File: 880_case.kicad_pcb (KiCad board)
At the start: 2 copper layers, 316.8 x 38 mm, 178 parts, among them CON1 BARREL_JACK, J1 RUN/STOP, J10 RS IN, J11 CP IN, J12 MA IN, J13 CB IN, J14 CY IN, J15 OH IN, J16 CH IN, J17 IN 1, J18 IN 2, J19 IN 3, J2 SYNC24 CLK, J20 IN 4, J21 MULT IN, J22 SUM, J23 JACK_STEREO, J24 JACK_TRS_SWITCHED, J3 ASSIGN 1, J4 ASSIGN 2, J5 BD IN, J6 SD IN, J7 LT IN, J8 MT IN, J9 HT IN, P1 CONN_02X03, P2 CONN_01X02, P3 CONN_02X05, P4 CONN_01X03, P5 CONN_01X04, P6 CONN_01X04, P7 CONN_01X03, P8 CONN_01X03, P9 CONN_01X03, Q1 MMBT3904, Q10 MMBT3904, Q11 MMBT3904, Q12 MMBT3904, Q13 MMBT3904, Q14 C945, Q15 A733, Q2 MMBT3904, Q3 MMBT3904, Q4 MMBT3904, Q5 MMBT3904, Q6 MMBT3904, Q7 MMBT3904, Q8 MMBT3904, Q9 MMBT3904, U1 74HC165, U2 74HC165, U3 VX078-500, U4 VX078-500, U5 4558, U6 4558, X1 MIDI OUT, X2 SYNC24

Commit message: working on second revision, about to move headhpone amp circuit to align board-to-board connectors
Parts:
- P3: footprint w_conn_strip:vasch_strip_5x2 -> w_conn_strip:vasch_strip_8x2
- U5, U6: footprint Housings_SSOP:TSSOP-8_3x3mm_Pitch0.65mm -> Housings_SSOP:TSSOP-8_4.4x3mm_Pitch0.65mm
- moved P5 25.4 mm to (263.6, 88.5)
- moved R67 25.4 mm to (258.6, 85.0)
- moved C17 24.1 mm to (258.4, 117.5)
- moved D21 23.3 mm to (255.9, 110.5)
- moved Q14 23.3 mm to (254.7, 114.5)
- moved Q15 23.3 mm to (251.7, 110.5)
- moved R59 23.3 mm to (254.4, 110.7)
- moved R61 23.3 mm to (251.7, 115.5)
- moved R62 23.3 mm to (252.7, 107.5)
- moved C18 23.3 mm to (262.9, 111.5)
- moved D20 23.3 mm to (257.4, 110.5)
- moved R58 23.3 mm to (257.4, 114.2)
- moved R63 23.3 mm to (256.6, 107.5)
- moved R64 23.3 mm to (256.6, 105.5)
- moved U6 22.6 mm to (260.4, 112.0)
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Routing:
- net Net-(P7-Pad2): track 21.8 -> 2.27 mm, vias 1 -> 0
- net Net-(J21-Pad2): track 33.2 -> 16.3 mm
- net Net-(P7-Pad1): track 12.0 -> 6.47 mm
- net -V: track 313.8 -> 317.9 mm, vias 4 -> 3
- net GND: track 88.0 -> 84.0 mm, vias 19 -> 17
- net Net-(C5-Pad1): track 41.8 -> 45.3 mm
- net Net-(C6-Pad2): track 8.50 -> 11.8 mm
- net +V: track 272.0 -> 274.2 mm
- net Net-(C15-Pad2): track 12.6 -> 10.6 mm
- net Net-(R1-Pad1): track 50.5 -> 52.2 mm
- net (no net): track 0.00 -> 1.63 mm
- net Net-(D20-Pad1): track 36.6 -> 35.8 mm
- net Net-(C12-Pad1): track 13.5 -> 14.3 mm
- net Net-(C16-Pad1): track 68.6 -> 67.8 mm
- net Net-(C11-Pad1): track 8.79 -> 9.47 mm
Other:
- board text added: "880 case board r1.1 6/2019"
- board text removed: "880 case board r1.0 2/2019"

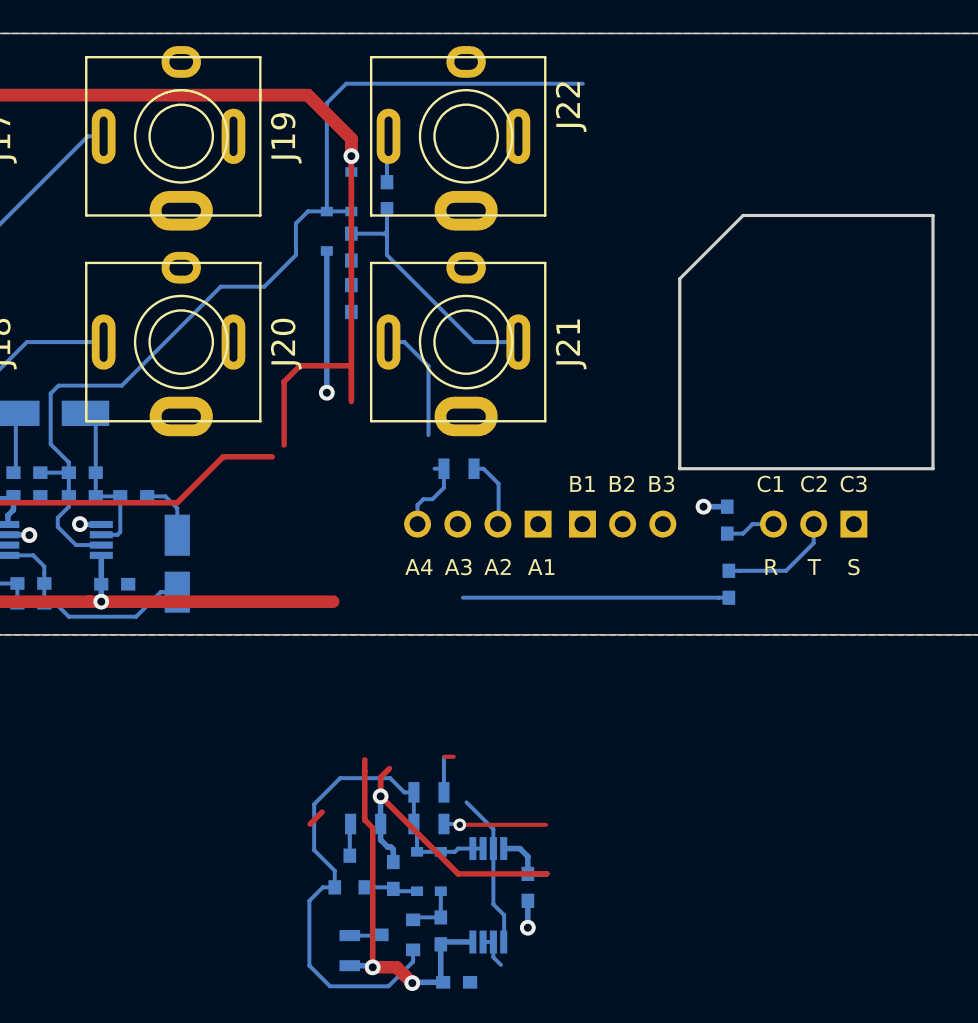
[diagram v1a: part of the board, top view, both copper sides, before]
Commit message: headphone amp components moved
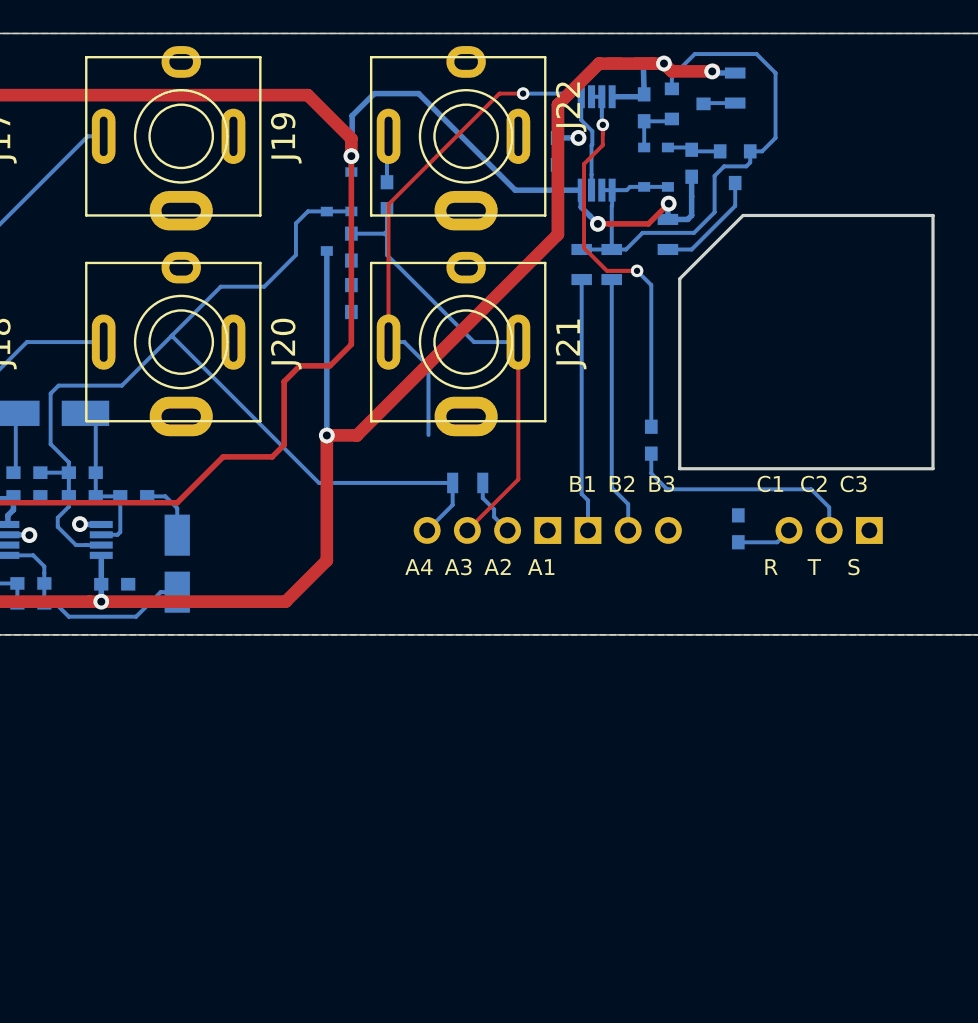
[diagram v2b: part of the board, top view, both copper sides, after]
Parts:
- moved R61 59.7 mm to (276.0, 61.0), turned to 270 degrees
- moved C17 59.0 mm to (269.2, 59.4), turned to 180 degrees
- moved Q14 55.6 mm to (273.0, 62.0), turned to 0 degrees
- moved R58 53.6 mm to (270.2, 62.2), turned to 270 degrees
- moved Q15 50.7 mm to (276.0, 66.0), turned to 270 degrees
- moved R59 48.8 mm to (273.2, 65.7), turned to 90 degrees
- moved U6 48.0 mm to (267.2, 64.5), turned to 90 degrees
- moved D21 47.2 mm to (271.8, 66.0), turned to 90 degrees
- moved C18 46.5 mm to (264.8, 65.0), turned to 90 degrees
- moved D20 46.3 mm to (270.2, 66.0), turned to 270 degrees
- moved R62 41.9 mm to (271.8, 70.2), turned to 90 degrees
- moved R63 36.6 mm to (266.3, 72.1), turned to 270 degrees
- moved R64 35.3 mm to (268.2, 72.1), turned to 270 degrees
- moved R57 10.3 mm to (270.7, 83.2), turned to 90 degrees
- moved P4 1.06 mm to (284.5, 88.9)
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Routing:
- net +V: track 274.2 -> 307.4 mm
- net Net-(J21-Pad3): track 17.3 -> 37.6 mm, vias 0 -> 1
- net Net-(P7-Pad2): track 2.27 -> 16.3 mm
- net Net-(J21-Pad2): track 16.3 -> 29.6 mm
- net Net-(P7-Pad1): track 6.47 -> 16.0 mm, vias 1 -> 0
- net -V: track 317.9 -> 327.2 mm, vias 3 -> 4
- net Net-(P4-Pad2): track 7.48 -> 14.8 mm
- net Net-(R57-Pad2): track 19.2 -> 24.9 mm, vias 0 -> 2
- net Net-(Q15-Pad3): track 2.02 -> 6.84 mm
- net Net-(C16-Pad1): track 67.8 -> 64.4 mm
- net GND: track 84.0 -> 82.1 mm, vias 17 -> 16
- net Net-(D20-Pad1): track 35.8 -> 37.4 mm
- net (no net): track 1.63 -> 0.00 mm
- net Net-(P5-Pad2): track 4.51 -> 3.71 mm

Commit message: more edits
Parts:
- G***: moved to F.Cu
- P3: value CONN_02X05 -> CONN_02X08
- moved P6 10.2 mm to (316.2, 88.9)
- moved C23 5.26 mm to (240.5, 85.8), turned to 180 degrees
- moved G*** 4.02 mm to (313.0, 74.0)
- moved R59 3.51 mm to (275.9, 63.4), turned to 180 degrees
- moved R51 2.55 mm to (238.5, 89.2)
- moved P8 0.61 mm to (318.8, 88.9)
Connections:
- P3 pad 11: (no net) -> Net-(P3-Pad11)
- P3 pad 12: (no net) -> Net-(P3-Pad12)
- P3 pad 13: (no net) -> Net-(P3-Pad13)
- P3 pad 14: (no net) -> Net-(P3-Pad14)
- P3 pad 15: (no net) -> Net-(P3-Pad15)
- P3 pad 16: (no net) -> Net-(P3-Pad16)
- U2 pad 6: Net-(U2-Pad6) -> GND
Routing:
- net Net-(J24-Pad1): track 13.8 -> 38.7 mm
- net Net-(J24-Pad3): track 44.4 -> 26.5 mm
- net Net-(J24-Pad4): track 13.6 -> 21.7 mm
- net Net-(C12-Pad1): track 14.3 -> 22.1 mm
- net -V: track 327.2 -> 334.0 mm, vias 4 -> 5
- net Net-(J21-Pad3): track 37.6 -> 30.9 mm
- net Net-(J24-Pad2): track 32.7 -> 26.2 mm
- net GND: track 82.1 -> 88.3 mm, vias 16 -> 17
- net Net-(D20-Pad1): track 37.4 -> 31.6 mm
- net +V: track 307.4 -> 302.9 mm
- net Net-(D21-Pad1): track 3.40 -> 4.95 mm
- net Net-(J23-Pad2): track 28.1 -> 26.8 mm
- net Net-(J23-Pad1): track 31.1 -> 30.6 mm

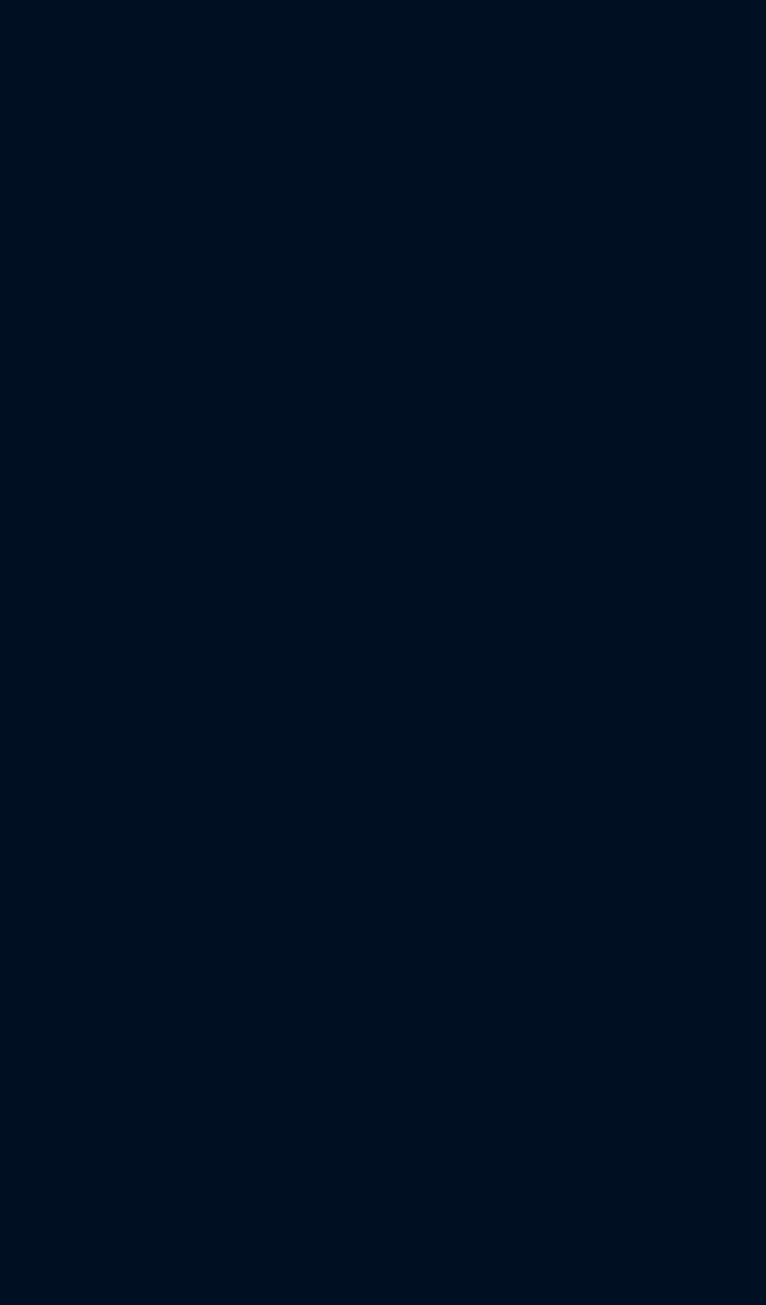
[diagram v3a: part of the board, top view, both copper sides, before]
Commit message: added power switch and balanced jack sub boards
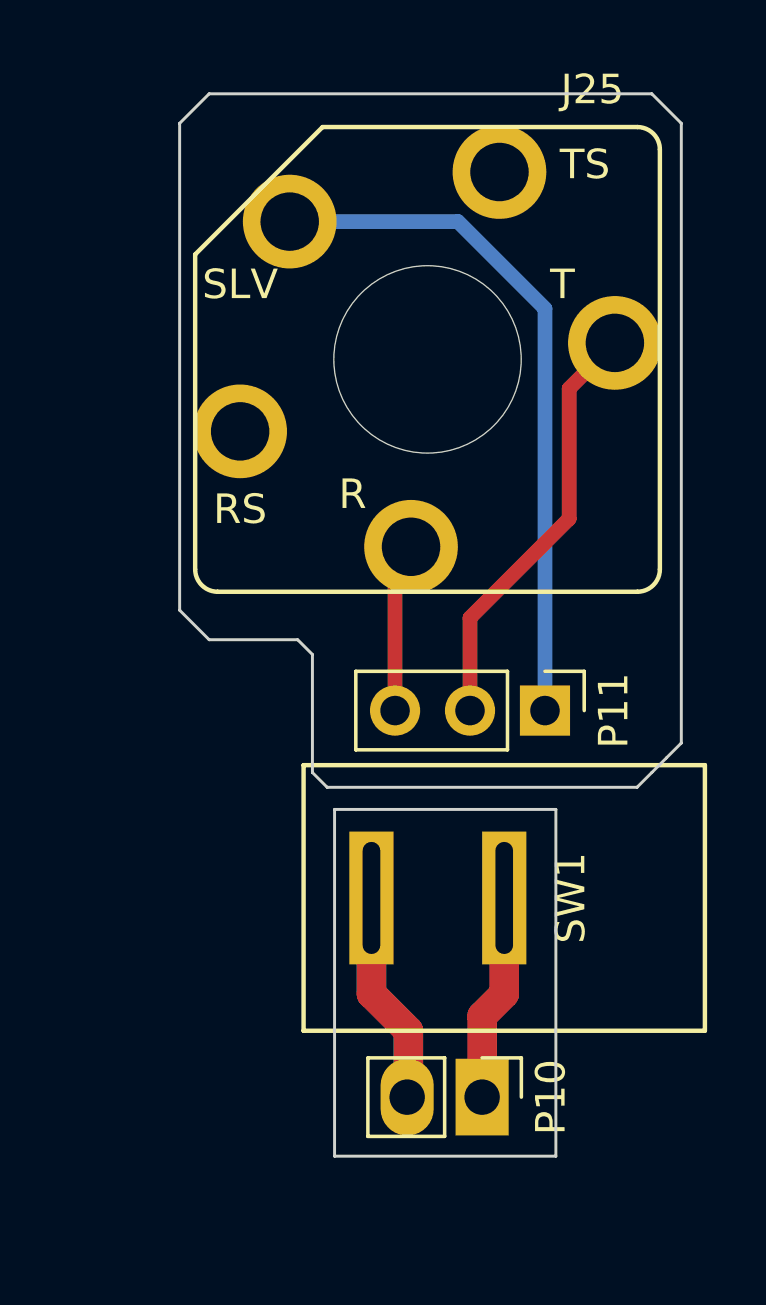
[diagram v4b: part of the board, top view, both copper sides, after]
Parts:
- added J25: JACK_STEREO, MyModules:11XPC-SWITCH_CRAFT, F.Cu at (354.9, 65.5)
- added P10: CONN_01X02, Pin_Headers:Pin_Header_Straight_1x02_Pitch2.54mm, F.Cu at (356.8, 90.5)
- added P11: CONN_01X03, Pin_Headers:Pin_Header_Straight_1x03_Pitch2.54mm, F.Cu at (358.9, 77.4)
- added SW1: SPST, MyModules:PR_PPR_ROCKER_SW, F.Cu at (357.5, 83.8)
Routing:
- net Net-(J25-Pad1): track 0.00 -> 23.5 mm
- net Net-(P10-Pad2): track 0.00 -> 14.5 mm
- net Net-(J25-Pad2): track 0.00 -> 14.5 mm
- net Net-(P10-Pad1): track 0.00 -> 14.1 mm
- net Net-(J25-Pad3): track 0.00 -> 5.77 mm
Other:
- board size 316.8 x 38 mm -> 351.5 x 39 mm
